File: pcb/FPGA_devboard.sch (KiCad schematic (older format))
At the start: 2 parts, among them X5 Conn_02x05_Odd_Even, X6 AC7020

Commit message: pinout changes
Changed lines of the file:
@@
 	4600 3200 4300 3200
 Wire Notes Line
-	950  4650 950  4350
+	1050 4650 1050 4350
 Wire Notes Line
-	950  4350 1850 4350
+	1050 4350 1800 4350
 Wire Notes Line
-	1850 4650 950  4650
+	1800 4650 1050 4650
 Wire Notes Line
 	5300 5450 4650 5450
@@
 	1800 3750 1800 3950
 Wire Notes Line
-	700  3950 700  3750
+	800  3950 800  3750
 Wire Notes Line
 	4600 3050 5250 3050
@@
 FPGA_HDMI_CLK+
 Wire Notes Line
-	1800 3950 700  3950
+	1800 3950 800  3950
 Wire Notes Line
-	700  3750 1800 3750
+	800  3750 1800 3750
 Text GLabel 4600 5800 2    50   BiDi ~ 0
 _FPGA_DS
@@
 _FPGA_INONLY_BUFF_OE
 Wire Notes Line
-	1850 4350 1850 4650
+	1800 4350 1800 4650
 Text GLabel 1800 5300 0    50   Output ~ 0
 FPGA_HDMI_CLK-

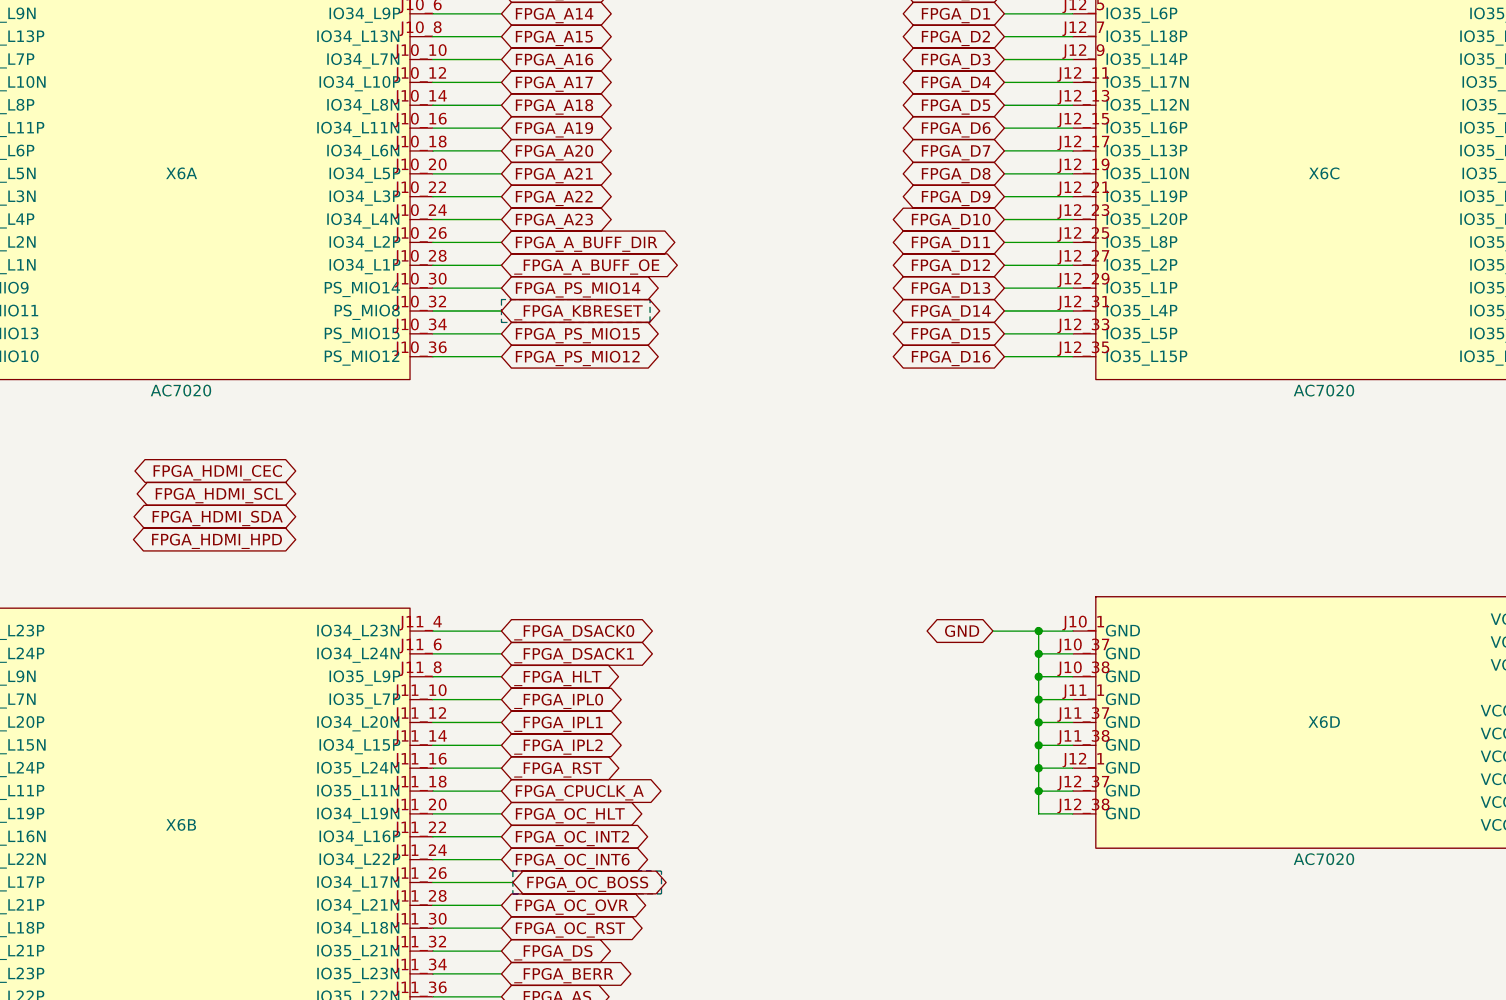
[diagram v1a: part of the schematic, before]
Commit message: more footprints assigned
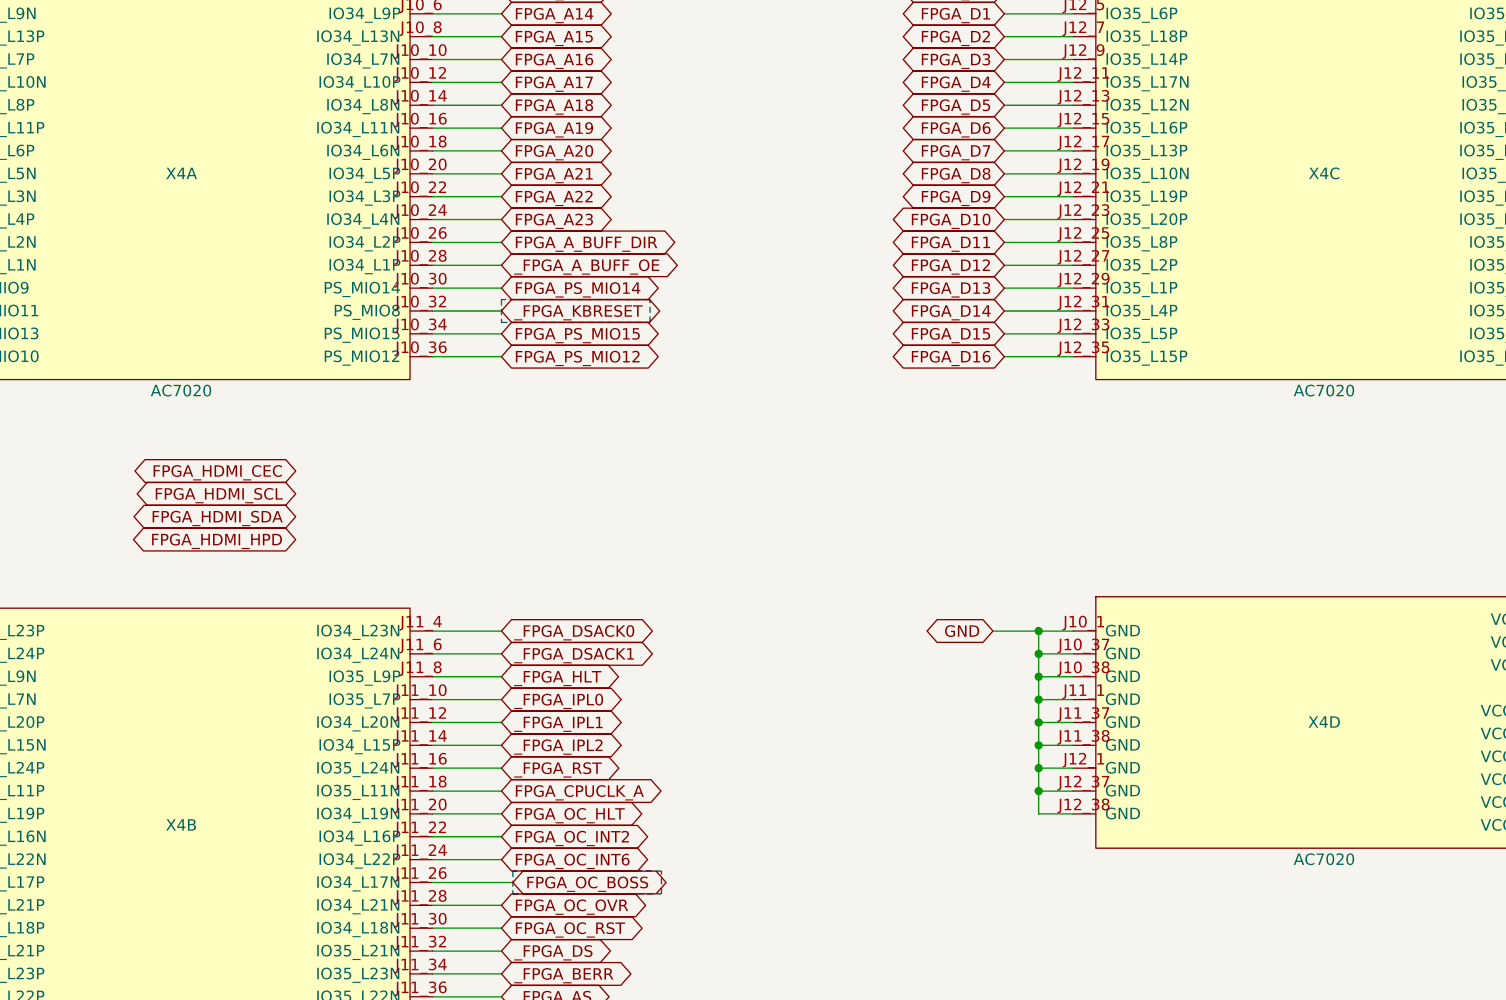
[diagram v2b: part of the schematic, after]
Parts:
- renumbered X6 to X4
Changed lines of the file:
@@
 $EndDescr
 $Comp
-L WM1200:AC7020 X6
+L WM1200:AC7020 X4
 U 1 1 5EB9A3F4
 P 3200 3300
-F 0 "X6" H 3200 4200 50  0000 C CNN
+F 0 "X4" H 3200 4200 50  0000 C CNN
 F 1 "AC7020" H 3200 3250 50  0000 C CNN
 F 2 "" H 3200 3300 50  0001 C CNN
@@
 $EndComp
 $Comp
-L WM1200:AC7020 X6
+L WM1200:AC7020 X4
 U 2 1 5EBA0B64
 P 3200 6100
-F 0 "X6" H 3200 6950 50  0000 C CNN
+F 0 "X4" H 3200 6950 50  0000 C CNN
 F 1 "AC7020" H 3200 6050 50  0000 C CNN
 F 2 "" H 3200 6100 50  0001 C CNN
@@
 $EndComp
 $Comp
-L WM1200:AC7020 X6
+L WM1200:AC7020 X4
 U 3 1 5EBA7395
 P 8200 3300
-F 0 "X6" H 8200 4200 50  0000 C CNN
+F 0 "X4" H 8200 4200 50  0000 C CNN
 F 1 "AC7020" H 8200 3250 50  0000 C CNN
 F 2 "" H 8200 3300 50  0001 C CNN
@@
 $EndComp
 $Comp
-L WM1200:AC7020 X6
+L WM1200:AC7020 X4
 U 4 1 5EBCCB73
 P 8200 5350
-F 0 "X6" H 8200 5900 50  0000 C CNN
+F 0 "X4" H 8200 5900 50  0000 C CNN
 F 1 "AC7020" H 8200 5300 50  0000 C CNN
 F 2 "" H 8200 5350 50  0001 C CNN

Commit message: More footprints assigned
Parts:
- X5: footprint (none) -> Connector_PinHeader_2.54mm:PinHeader_2x05_P2.54mm_Vertical
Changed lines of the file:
@@
 F 0 "X5" H 3200 7417 50  0000 C CNN
 F 1 "Conn_02x05_Odd_Even" H 3200 7326 50  0000 C CNN
-F 2 "" H 3150 7000 50  0001 C CNN
+F 2 "Connector_PinHeader_2.54mm:PinHeader_2x05_P2.54mm_Vertical" H 3150 7000 50  0001 C CNN
 F 3 "~" H 3150 7000 50  0001 C CNN
 	1    3150 7000

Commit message: working on pcb
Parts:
- X4: footprint (none) -> WM1200:ac7020
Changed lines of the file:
@@
 F 0 "X4" H 3200 4200 50  0000 C CNN
 F 1 "AC7020" H 3200 3250 50  0000 C CNN
-F 2 "" H 3200 3300 50  0001 C CNN
+F 2 "WM1200:ac7020" H 3200 3300 50  0001 C CNN
 F 3 "" H 3200 3300 50  0001 C CNN
 	1    3200 3300
@@
 F 0 "X4" H 3200 6950 50  0000 C CNN
 F 1 "AC7020" H 3200 6050 50  0000 C CNN
-F 2 "" H 3200 6100 50  0001 C CNN
+F 2 "WM1200:ac7020" H 3200 6100 50  0001 C CNN
 F 3 "" H 3200 6100 50  0001 C CNN
 	2    3200 6100
@@
 F 0 "X4" H 8200 4200 50  0000 C CNN
 F 1 "AC7020" H 8200 3250 50  0000 C CNN
-F 2 "" H 8200 3300 50  0001 C CNN
+F 2 "WM1200:ac7020" H 8200 3300 50  0001 C CNN
 F 3 "" H 8200 3300 50  0001 C CNN
 	3    8200 3300
@@
 F 0 "X4" H 8200 5900 50  0000 C CNN
 F 1 "AC7020" H 8200 5300 50  0000 C CNN
-F 2 "" H 8200 5350 50  0001 C CNN
+F 2 "WM1200:ac7020" H 8200 5350 50  0001 C CNN
 F 3 "" H 8200 5350 50  0001 C CNN
 	4    8200 5350

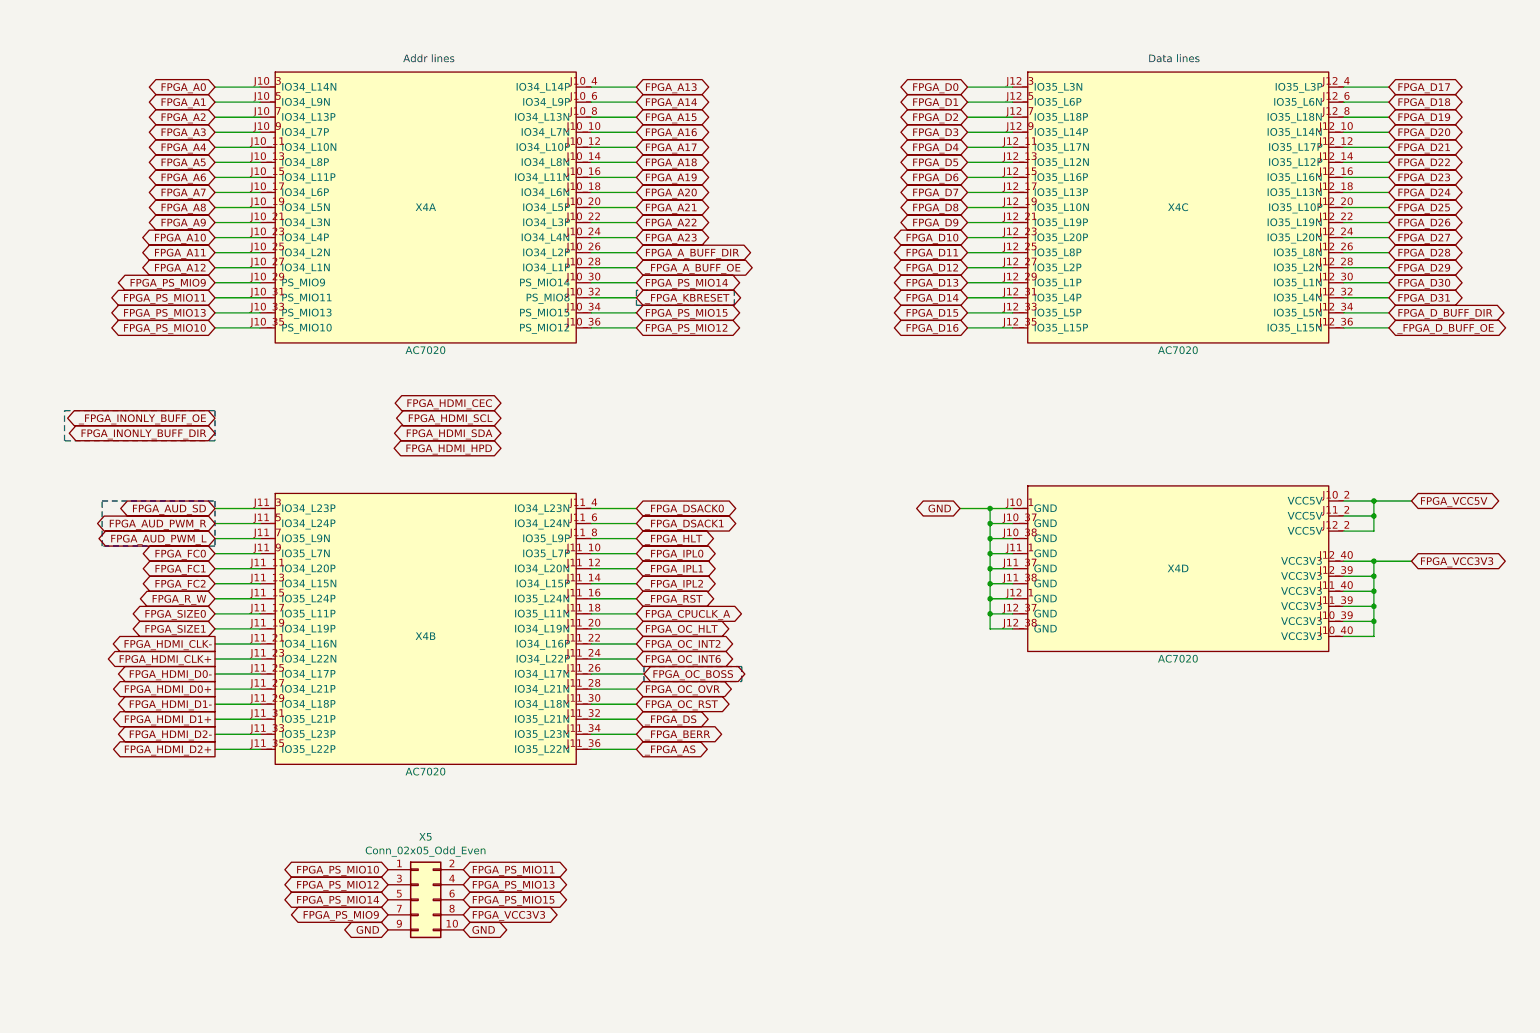
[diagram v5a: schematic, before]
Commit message: Buffers power scheme rework in progress, re-annotate board
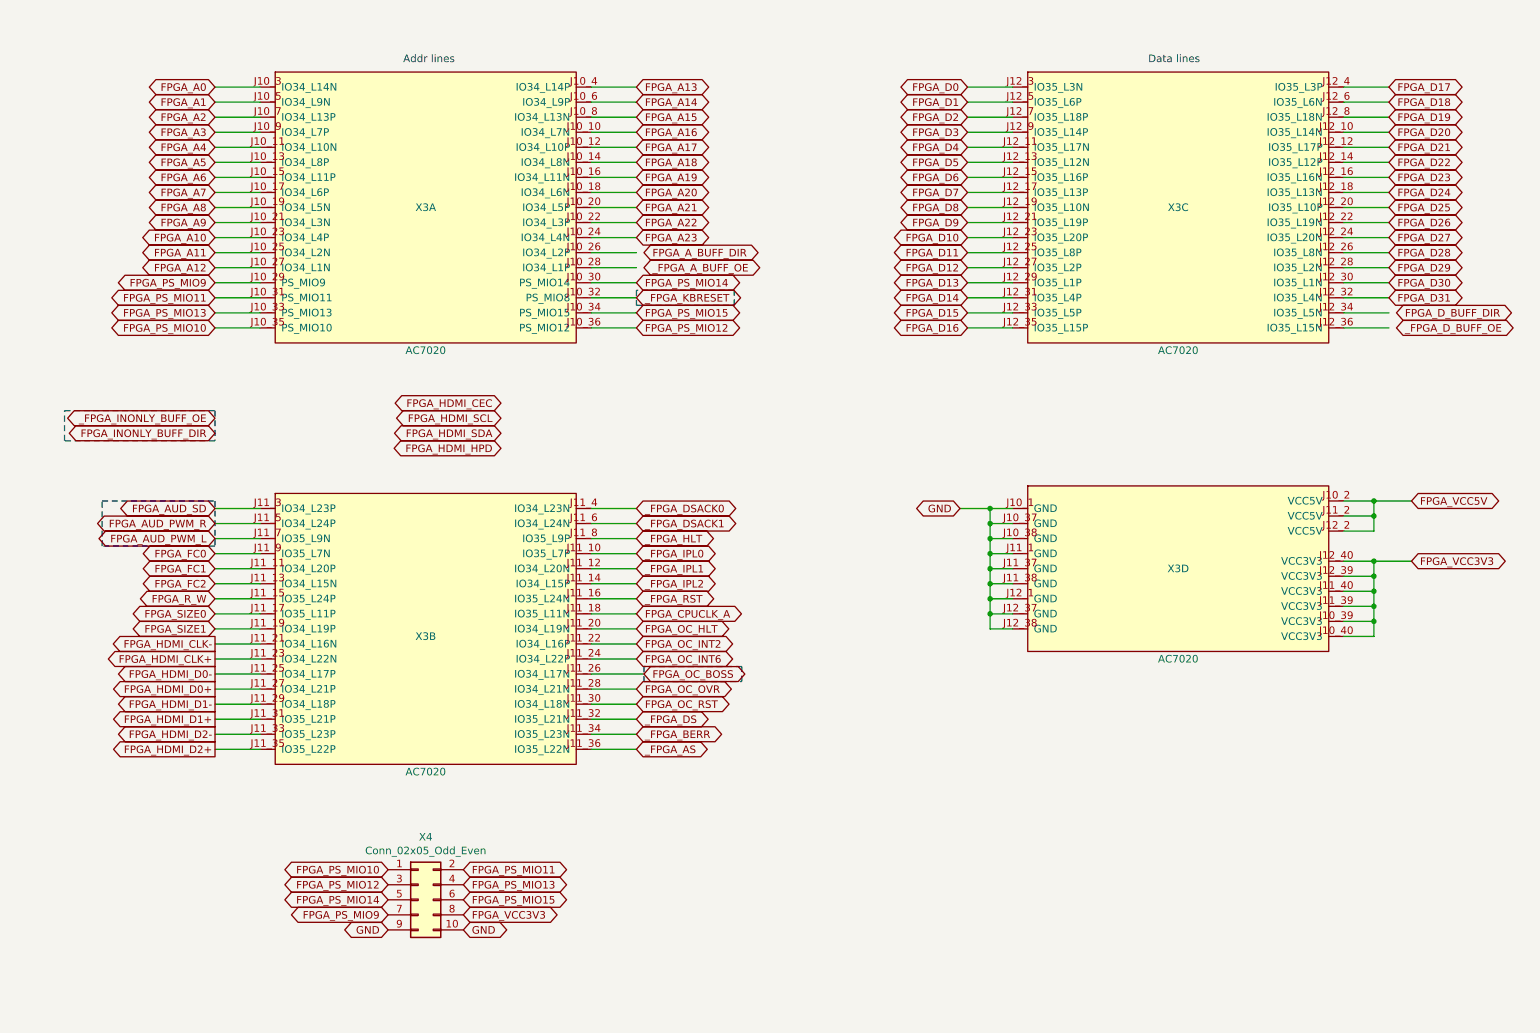
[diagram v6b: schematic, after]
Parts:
- renumbered X4 to X3, X5 to X4
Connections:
- net FPGA_A_BUFF_DIR: no longer X3.J10_26 (IO34_L2P)
- net FPGA_D_BUFF_DIR: no longer X3.J12_34 (IO35_L5N)
- net _FPGA_A_BUFF_OE: no longer X3.J10_28 (IO34_L1P)
- net _FPGA_D_BUFF_OE: no longer X3.J12_36 (IO35_L15N)
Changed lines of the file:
@@
 $Descr A4 11693 8268
 encoding utf-8
-Sheet 11 11
+Sheet 10 11
 Title "Wishmaster 1200"
 Date ""
@@
 $EndDescr
 $Comp
-L WM1200:AC7020 X4
+L WM1200:AC7020 X3
 U 1 1 5EB9A3F4
 P 3200 3300
-F 0 "X4" H 3200 4200 50  0000 C CNN
+F 0 "X3" H 3200 4200 50  0000 C CNN
 F 1 "AC7020" H 3200 3250 50  0000 C CNN
 F 2 "WM1200:ac7020" H 3200 3300 50  0001 C CNN
@@
 $EndComp
 $Comp
-L WM1200:AC7020 X4
+L WM1200:AC7020 X3
 U 2 1 5EBA0B64
 P 3200 6100
-F 0 "X4" H 3200 6950 50  0000 C CNN
+F 0 "X3" H 3200 6950 50  0000 C CNN
 F 1 "AC7020" H 3200 6050 50  0000 C CNN
 F 2 "WM1200:ac7020" H 3200 6100 50  0001 C CNN
@@
 $EndComp
 $Comp
-L WM1200:AC7020 X4
+L WM1200:AC7020 X3
 U 3 1 5EBA7395
 P 8200 3300
-F 0 "X4" H 8200 4200 50  0000 C CNN
+F 0 "X3" H 8200 4200 50  0000 C CNN
 F 1 "AC7020" H 8200 3250 50  0000 C CNN
 F 2 "WM1200:ac7020" H 8200 3300 50  0001 C CNN
@@
 $EndComp
 $Comp
-L WM1200:AC7020 X4
+L WM1200:AC7020 X3
 U 4 1 5EBCCB73
 P 8200 5350
-F 0 "X4" H 8200 5900 50  0000 C CNN
+F 0 "X3" H 8200 5900 50  0000 C CNN
 F 1 "AC7020" H 8200 5300 50  0000 C CNN
 F 2 "WM1200:ac7020" H 8200 5350 50  0001 C CNN
@@
 Text GLabel 4600 2600 2    50   BiDi ~ 0
 FPGA_A23
-Text GLabel 4600 2700 2    50   BiDi ~ 0
+Text GLabel 4650 2700 2    50   BiDi ~ 0
 FPGA_A_BUFF_DIR
-Text GLabel 4600 2800 2    50   BiDi ~ 0
+Text GLabel 4650 2800 2    50   BiDi ~ 0
 _FPGA_A_BUFF_OE
 Text GLabel 6800 1600 0    50   BiDi ~ 0
@@
 Text GLabel 9600 3000 2    50   BiDi ~ 0
 FPGA_D31
-Text GLabel 9600 3100 2    50   BiDi ~ 0
+Text GLabel 9650 3100 2    50   BiDi ~ 0
 FPGA_D_BUFF_DIR
-Text GLabel 9600 3200 2    50   BiDi ~ 0
+Text GLabel 9650 3200 2    50   BiDi ~ 0
 _FPGA_D_BUFF_OE
 Text GLabel 1800 4600 0    50   BiDi ~ 0
@@
 	4300 5100 4600 5100
 $Comp
-L Connector_Generic:Conn_02x05_Odd_Even X5
+L Connector_Generic:Conn_02x05_Odd_Even X4
 U 1 1 5E864C32
 P 3150 7000
-F 0 "X5" H 3200 7417 50  0000 C CNN
+F 0 "X4" H 3200 7417 50  0000 C CNN
 F 1 "Conn_02x05_Odd_Even" H 3200 7326 50  0000 C CNN
 F 2 "Connector_PinHeader_2.54mm:PinHeader_2x05_P2.54mm_Vertical" H 3150 7000 50  0001 C CNN
